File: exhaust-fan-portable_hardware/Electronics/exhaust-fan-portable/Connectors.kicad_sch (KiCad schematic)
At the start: 6 parts, among them J1 Conn_01x03_Pin, J2 Conn_01x04_Pin, J3 Conn_01x03_Pin, J4 Conn_01x04_Pin, J5 Conn_01x03_Pin, J6 Barrel_Jack_MountingPin

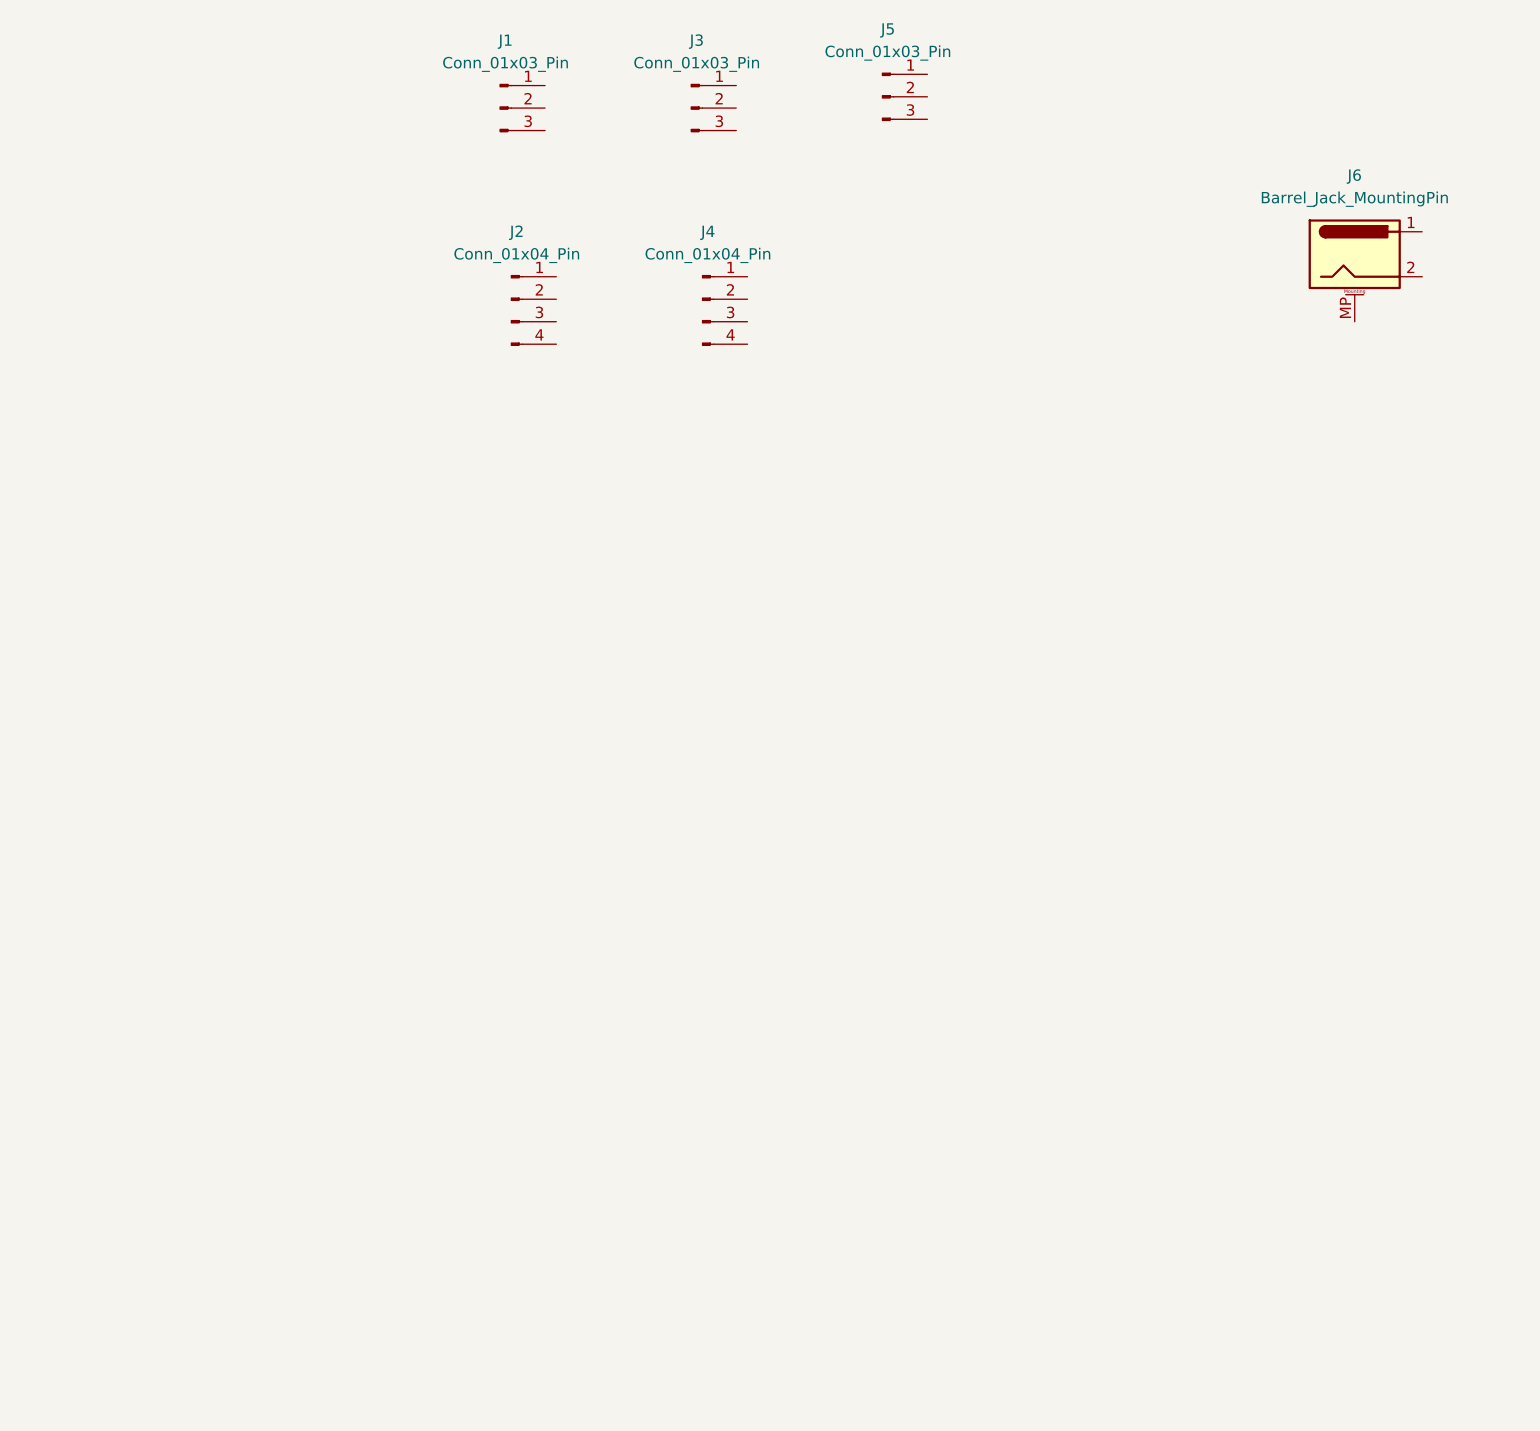
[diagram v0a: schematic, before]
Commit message: layed out rough schematic and added sensor comparison
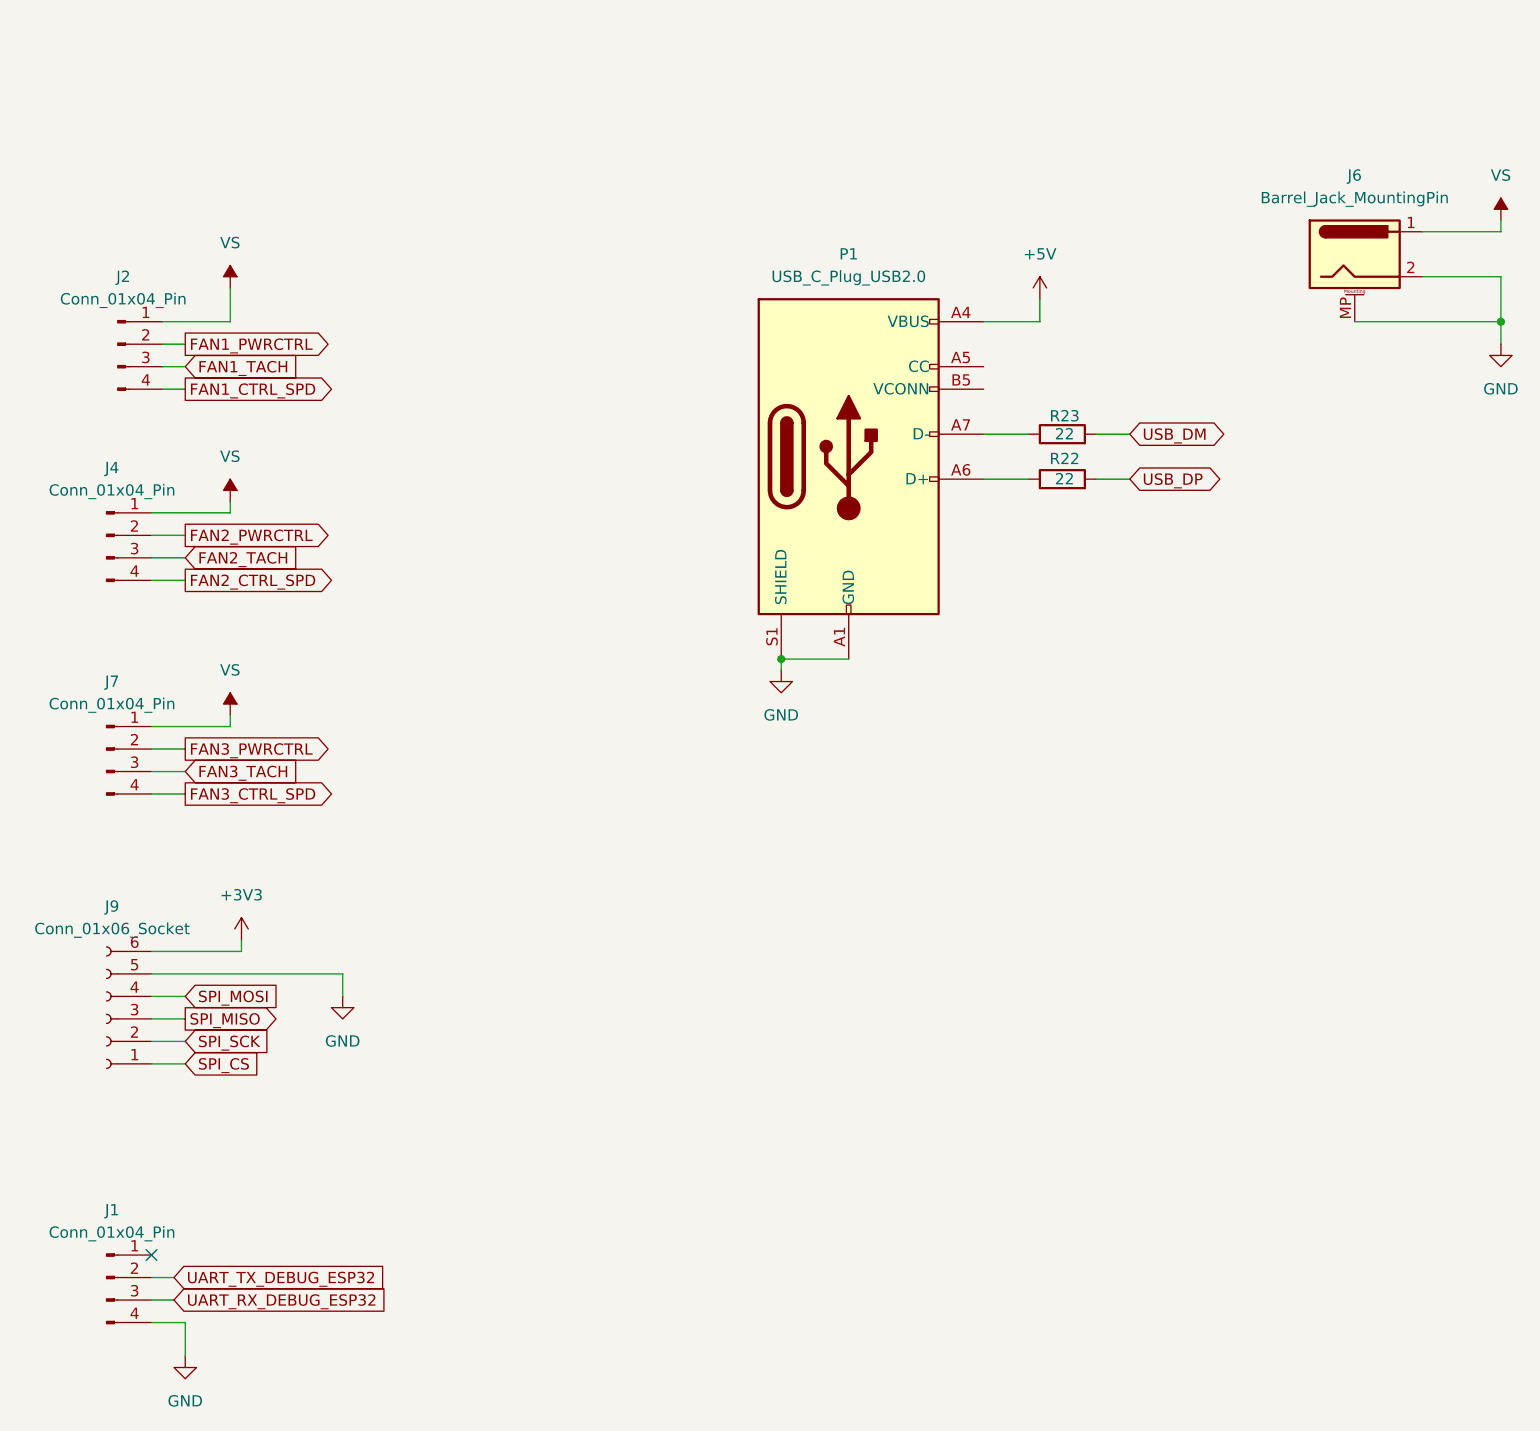
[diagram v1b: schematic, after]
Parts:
- removed J1, J3, J5: Conn_01x03_Pin, symbol Connector:Conn_01x03_Pin
- added J1, J7: Conn_01x04_Pin, symbol Connector:Conn_01x04_Pin
- added J9: Conn_01x06_Socket, symbol Connector:Conn_01x06_Socket
- added P1: USB_C_Plug_USB2.0, symbol Connector:USB_C_Plug_USB2.0
- added R22, R23: 22, symbol Device:R
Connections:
- net VS: now reaches J6.1
- net VS: now also J2.1 (Pin_1), J4.1 (Pin_1), J7.1 (Pin_1)
- net GND: now reaches J6.2
- net GND: now also J6.MP (MountPin), J1.4 (Pin_4), J9.5 (Pin_5), P1.A1 (GND), P1.A12 (GND), P1.B1 (GND), P1.B12 (GND), P1.S1 (SHIELD)
- net FAN2_PWRCTRL: now reaches J4.2 (Pin_2)
- net FAN2_TACH: now reaches J4.3 (Pin_3)
- net FAN2_CTRL_SPD: now reaches J4.4 (Pin_4)
- net FAN1_PWRCTRL: now reaches J2.2 (Pin_2)
- net FAN1_TACH: now reaches J2.3 (Pin_3)
- net FAN1_CTRL_SPD: now reaches J2.4 (Pin_4)
- new net: P1.A6 (D+), R22.1
- new net: P1.A7 (D-), R23.1
- new net +3V3: J9.6 (Pin_6)
- new net +5V: P1.A4 (VBUS), P1.A9 (VBUS), P1.B4 (VBUS), P1.B9 (VBUS)
- new net FAN3_CTRL_SPD: J7.4 (Pin_4)
- new net FAN3_PWRCTRL: J7.2 (Pin_2)
- new net FAN3_TACH: J7.3 (Pin_3)
- new net SPI_CS: J9.1 (Pin_1)
- new net SPI_MISO: J9.3 (Pin_3)
- new net SPI_MOSI: J9.4 (Pin_4)
- new net SPI_SCK: J9.2 (Pin_2)
- new net UART_RX_DEBUG_ESP32: J1.3 (Pin_3)
- new net UART_TX_DEBUG_ESP32: J1.2 (Pin_2)
- new net USB_DM: R23.2
- new net USB_DP: R22.2
- no-connect marks 0 -> 1
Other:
- moved on the sheet: J2, J4

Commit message: fixed case design
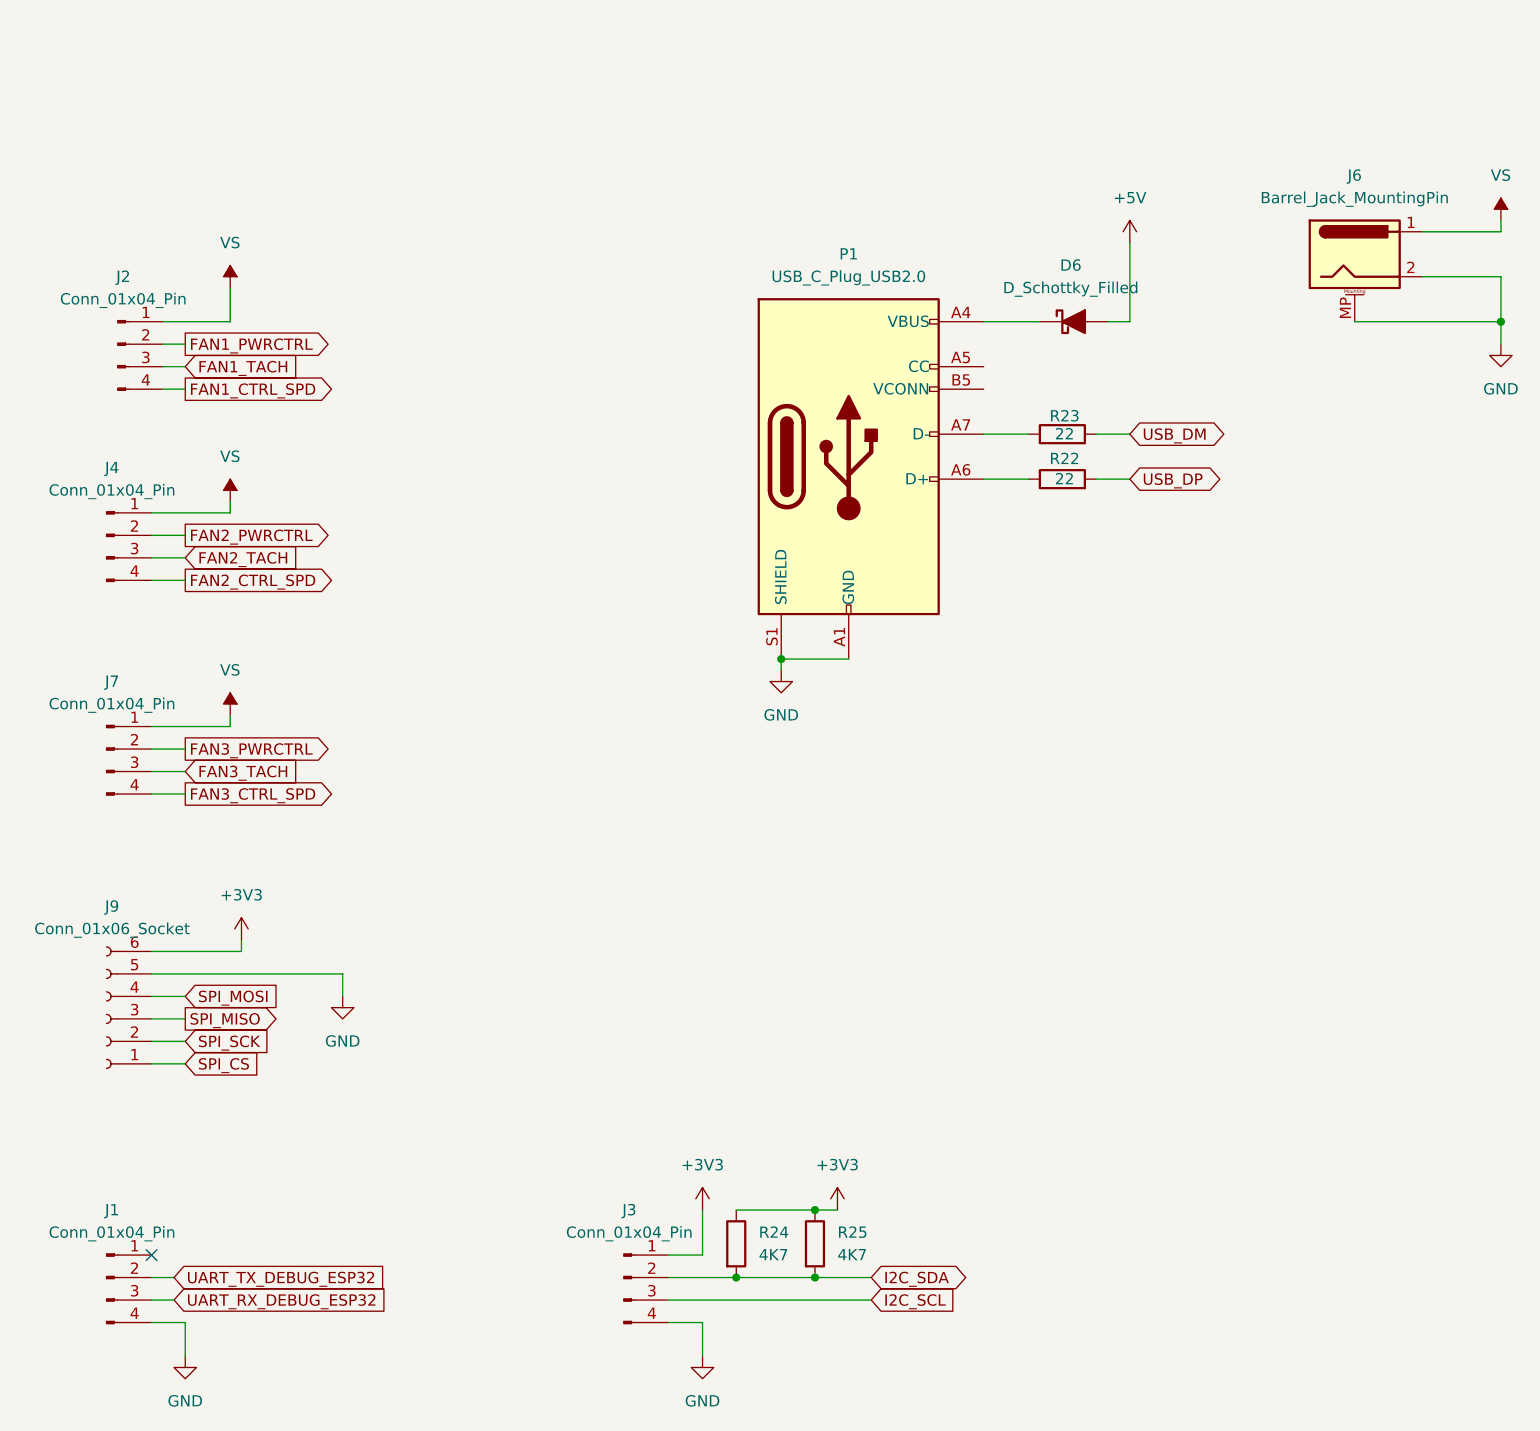
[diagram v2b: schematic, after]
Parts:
- added D6: D_Schottky_Filled, Diode_SMD:D_0603_1608Metric_Pad1.05x0.95mm_HandSolder, symbol Device:D_Schottky_Filled
- added J3: Conn_01x04_Pin, Connector_PinHeader_2.54mm:PinHeader_1x04_P2.54mm_Vertical, symbol Connector:Conn_01x04_Pin
- added R24, R25: 4K7, Resistor_SMD:R_0603_1608Metric_Pad0.98x0.95mm_HandSolder, symbol Device:R
- J1, J2, J4, J7: footprint (none) -> Connector_PinHeader_2.54mm:PinHeader_1x04_P2.54mm_Vertical
- J6: footprint (none) -> Connector_BarrelJack:BarrelJack_Horizontal
- J9: footprint (none) -> Connector_PinSocket_2.54mm:PinSocket_1x06_P2.54mm_Vertical
- P1: footprint (none) -> Connector_USB:USB_C_Receptacle_G-Switch_GT-USB-7010ASV
- R22, R23: footprint (none) -> Resistor_SMD:R_0603_1608Metric_Pad0.98x0.95mm_HandSolder
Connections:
- net +3V3: now also J3.1 (Pin_1), R24.1, R25.1
- net +5V: now also D6.2 (A); no longer P1.A4 (VBUS), P1.A9 (VBUS), P1.B4 (VBUS), P1.B9 (VBUS)
- net GND: now also J3.4 (Pin_4)
- new net: D6.1 (K), P1.A4 (VBUS), P1.A9 (VBUS), P1.B4 (VBUS), P1.B9 (VBUS)
- new net I2C_SCL: J3.3 (Pin_3)
- new net I2C_SDA: J3.2 (Pin_2), R24.2, R25.2
